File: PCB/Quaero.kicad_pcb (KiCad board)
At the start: 2 copper layers, 170.5 x 135.2 mm, 61 parts, among them J1 USB_C_Receptacle_USB2.0_16P, J2 OLED_128x32, J5 Conn_01x02, SW2 SW_SPDT

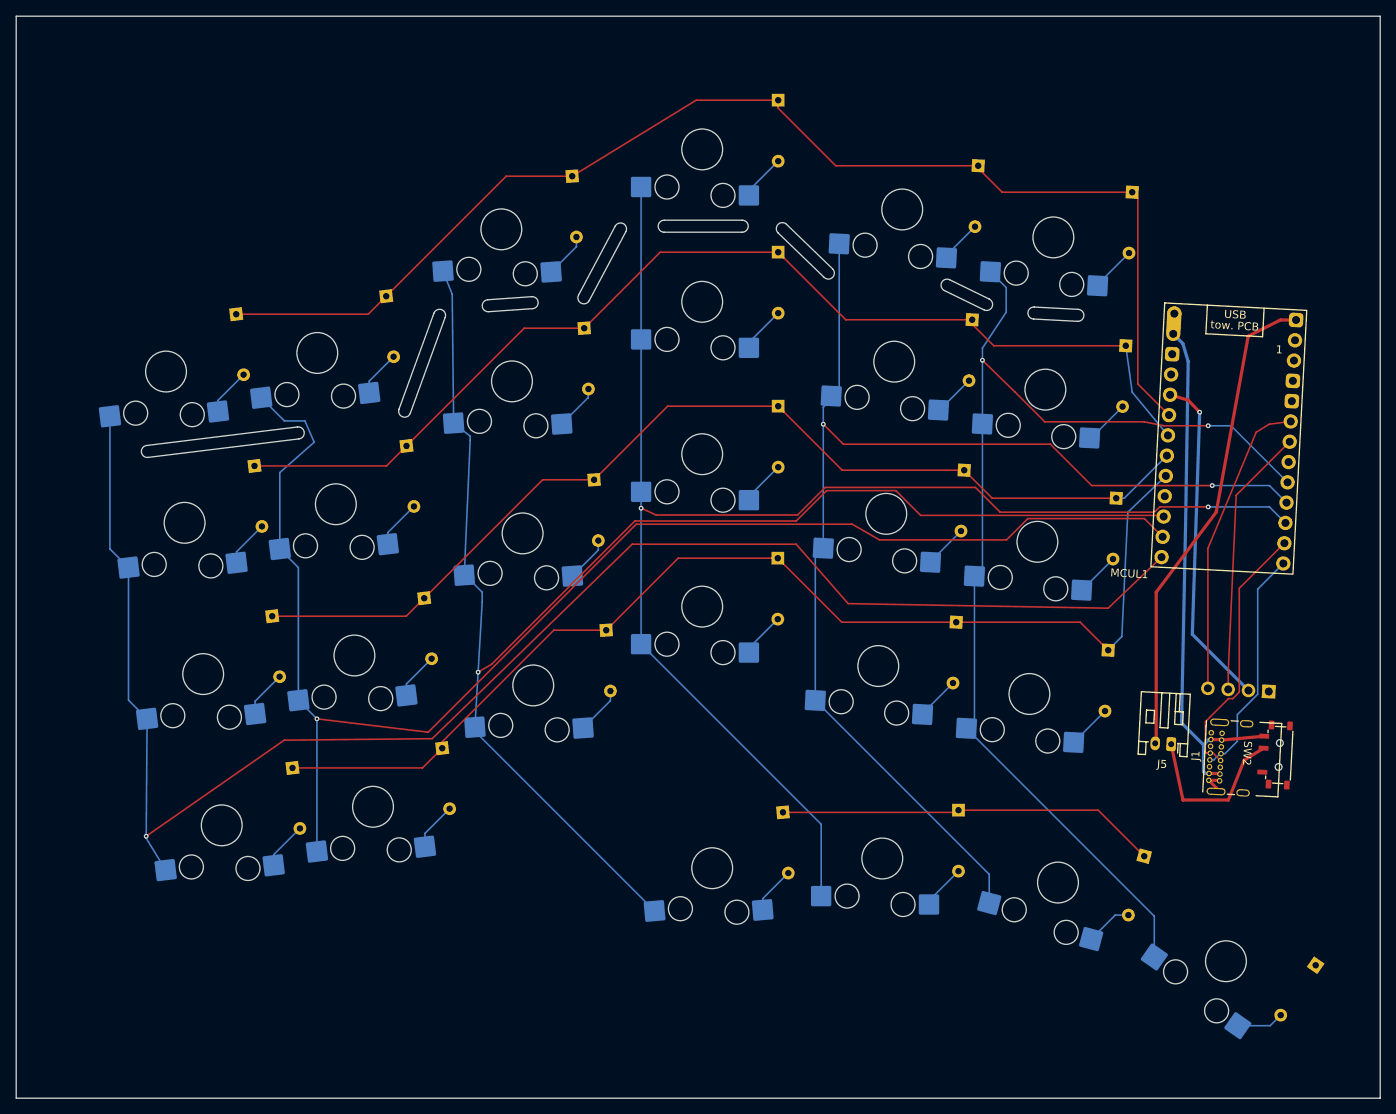
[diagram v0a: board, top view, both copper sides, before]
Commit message: Left side partial routing attempt 4
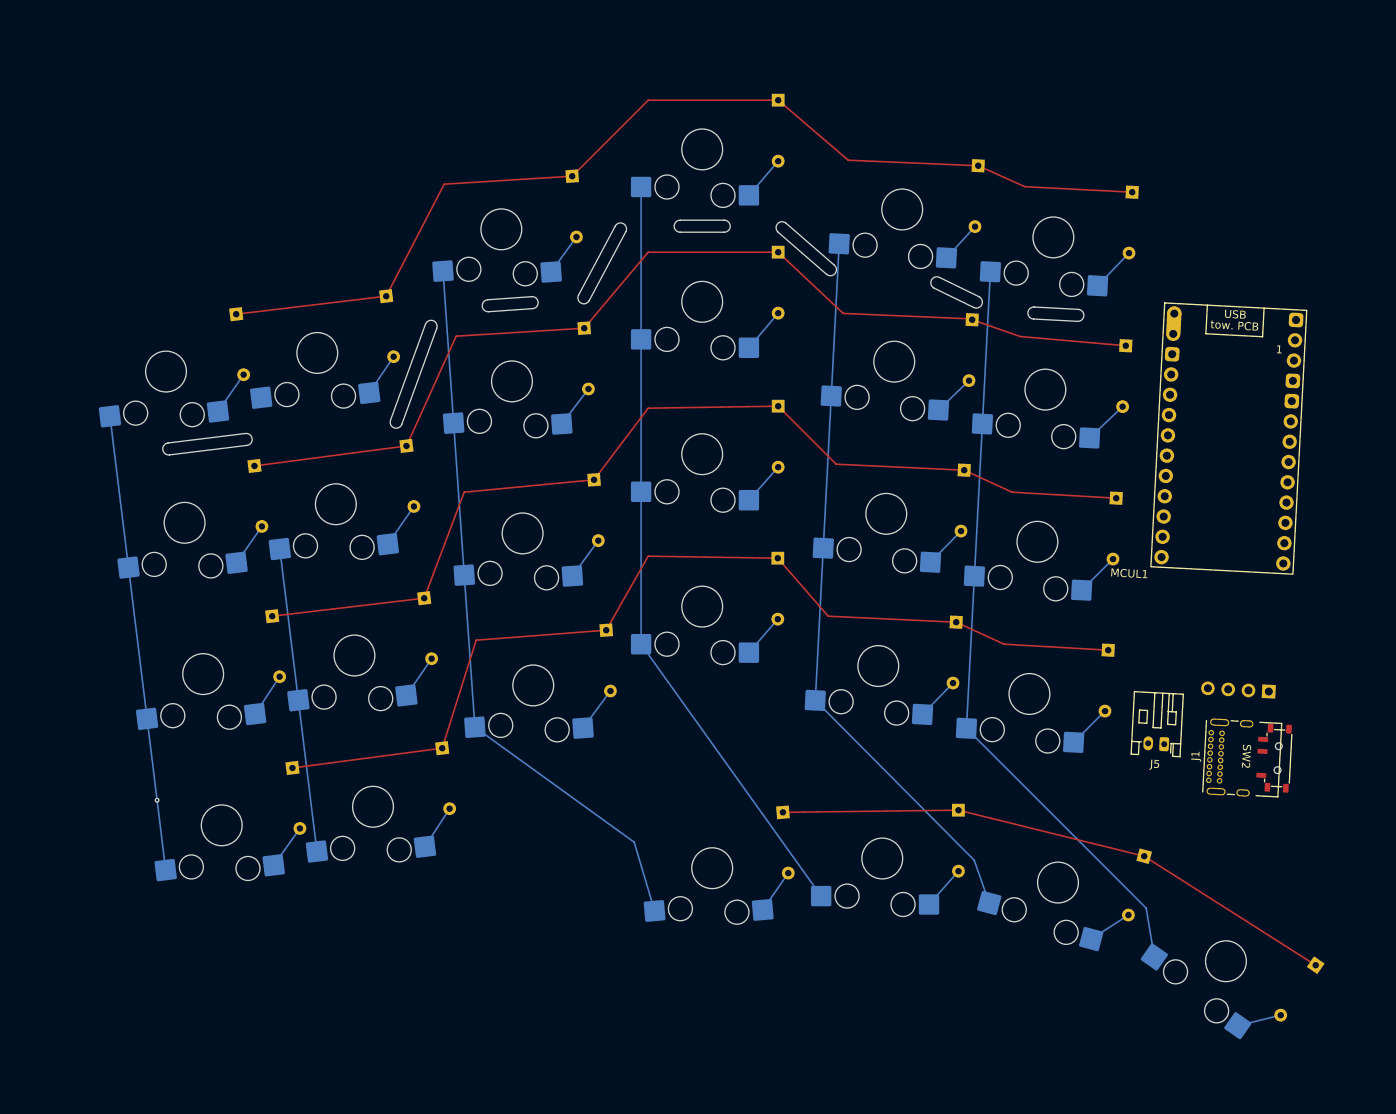
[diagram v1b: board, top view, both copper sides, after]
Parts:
- moved J5 0.87 mm to (153.0, 131.5)
- moved SW2 0.42 mm to (167.2, 133.2)
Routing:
- net LCol-1: track 205.8 -> 57.1 mm
- net LCol-2: track 183.7 -> 38.1 mm, vias 1 -> 0
- net LCol-3: track 187.8 -> 90.7 mm, vias 1 -> 0
- net LCol-4: track 182.6 -> 95.9 mm, vias 2 -> 0
- net PWR_Positive: track 66.6 -> 0.00 mm
- net LCol-5: track 154.6 -> 91.0 mm, vias 2 -> 0
- net PWR_Negative: track 60.5 -> 0.00 mm
- net LCol-6: track 142.2 -> 95.1 mm, vias 2 -> 0
- net +3.3V: track 42.1 -> 0.00 mm, vias 1 -> 0
- net Net-(J2-SDA): track 37.8 -> 0.00 mm
- net Net-(J2-SCL): track 33.7 -> 0.00 mm
- net RX: track 33.0 -> 0.00 mm
- net LRow-1: track 157.1 -> 128.0 mm
- net TX: track 29.0 -> 0.00 mm
- net LRow-5: track 47.6 -> 71.3 mm
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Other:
- board size 170.5 x 135.2 mm -> 115.1 x 29.3 mm

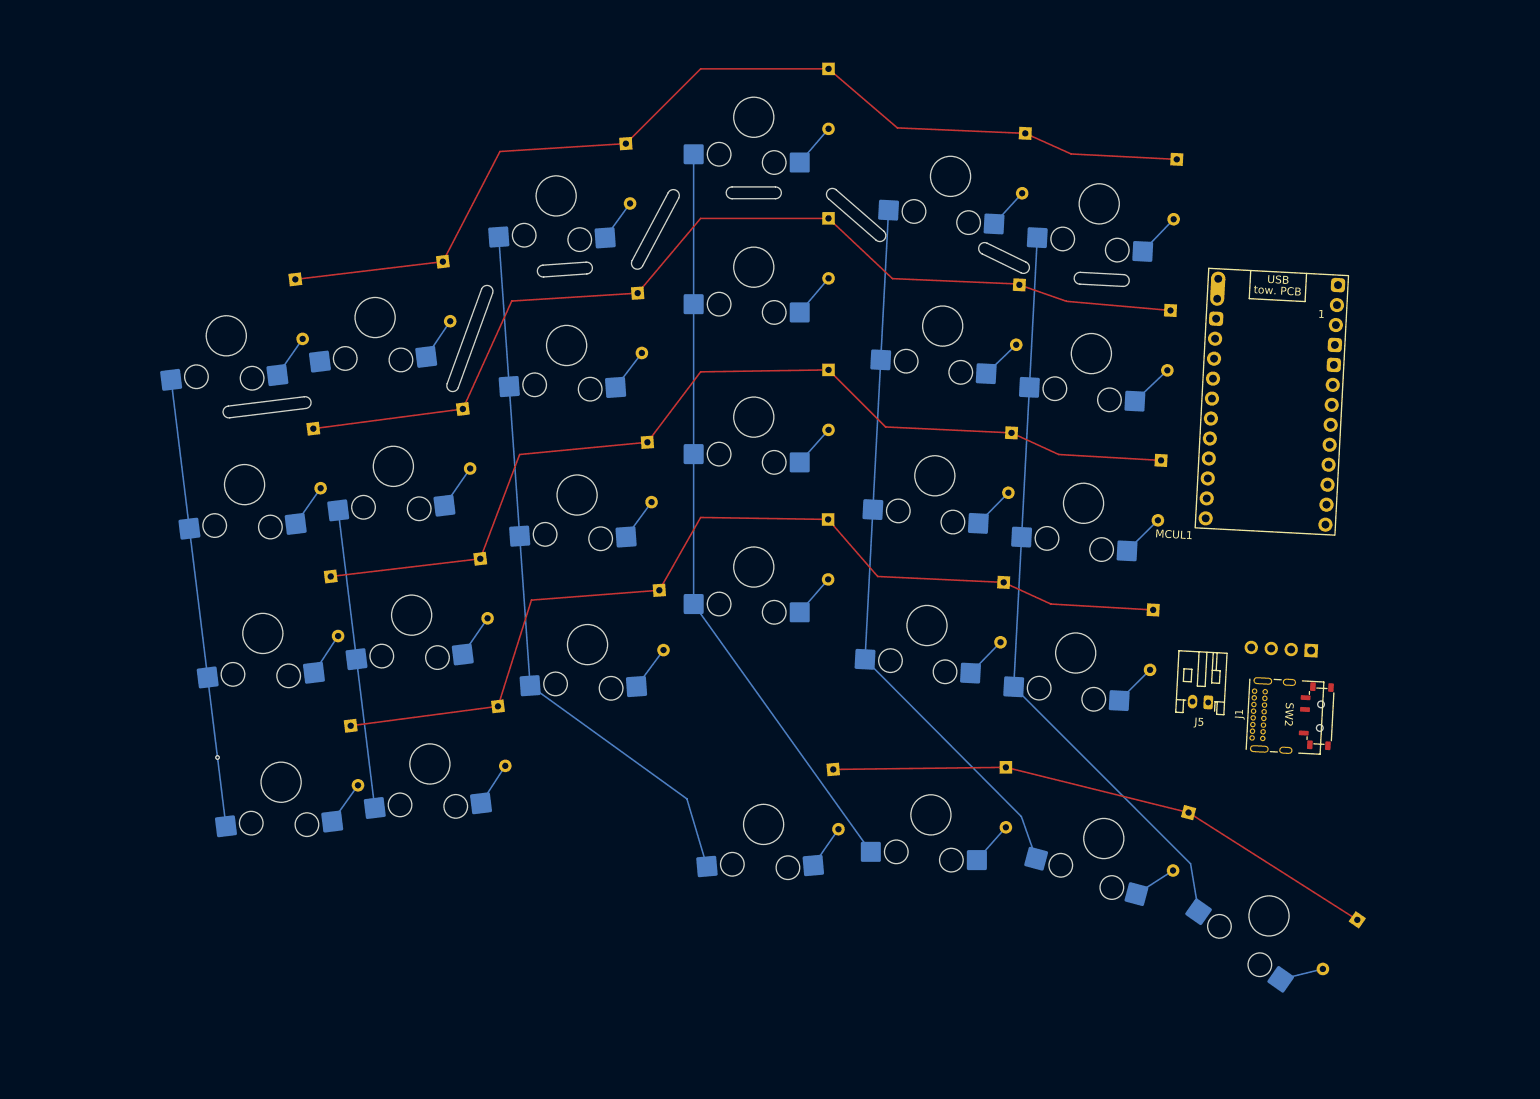
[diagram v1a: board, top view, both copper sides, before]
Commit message: Updated to RP2040, routing columns attempt 1
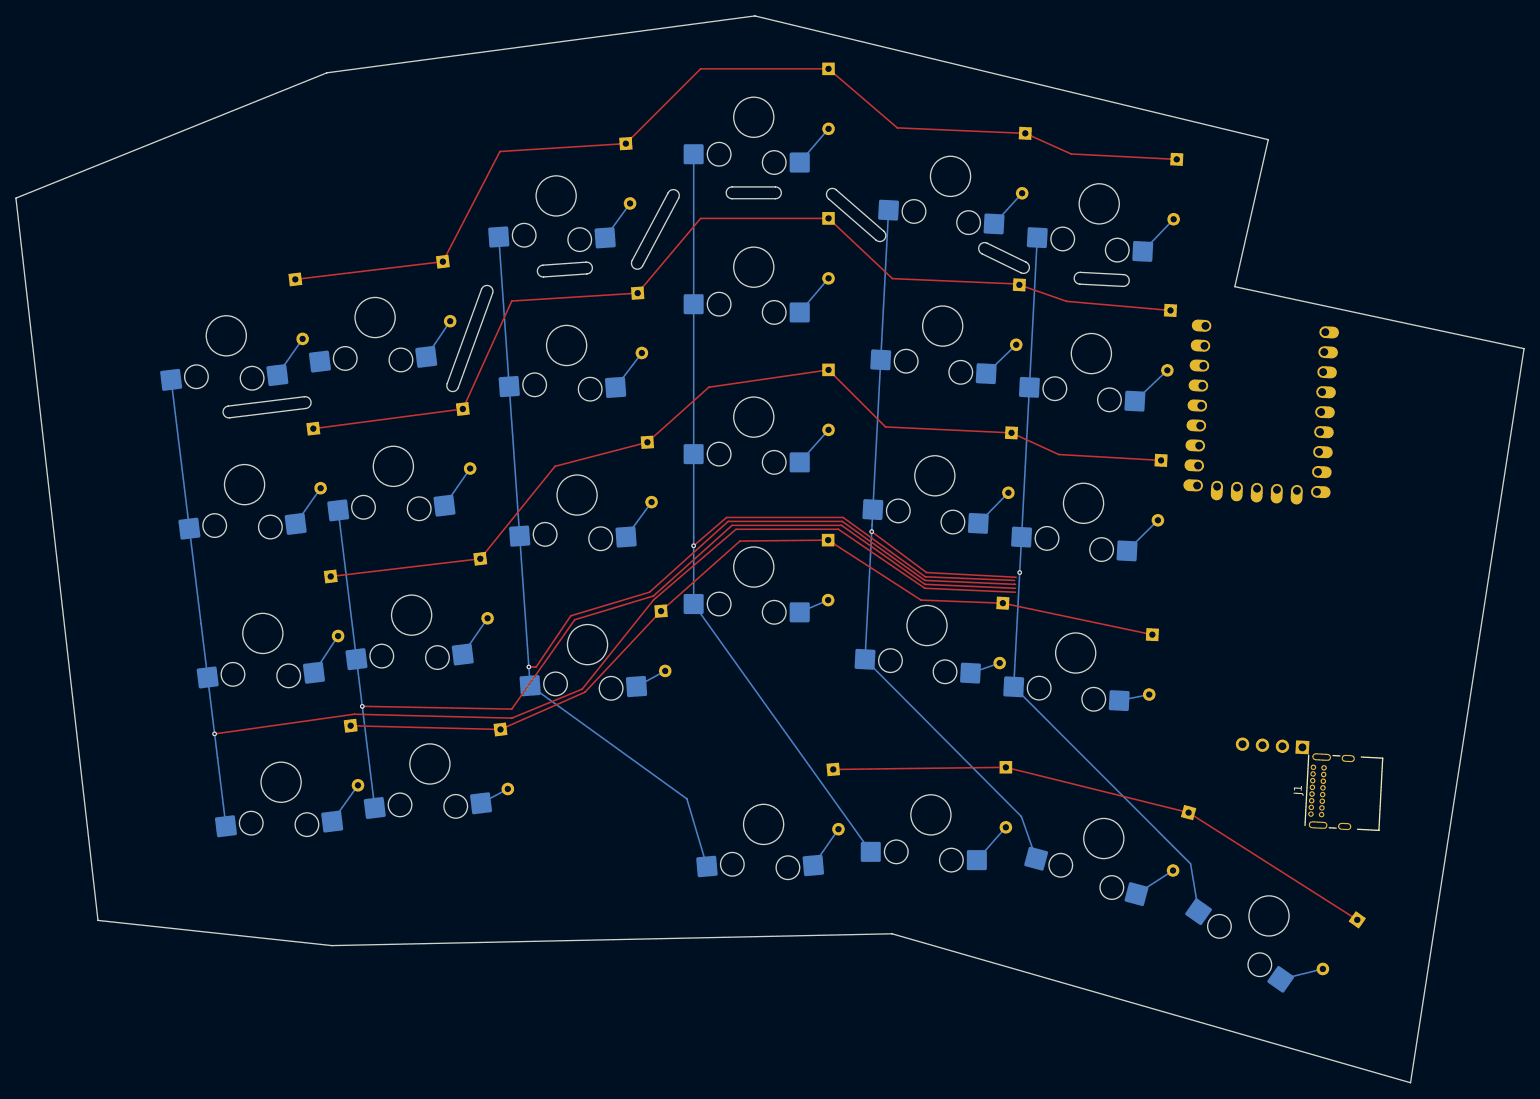
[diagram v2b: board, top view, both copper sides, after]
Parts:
- removed J5: Conn_01x02, Connector_JST:JST_PH_S2B-PH-K_1x02_P2.00mm_Horizontal
- removed MCUL1: SuperMini nRF52840, marbastlib-xp-promicroish:SuperMini_nRF52840_AH_USBdn
- removed SW2: SW_SPDT, marbastlib-various:SW_MSK12C02-HB
- added U1: RP2040_Zero, ScottoKeebs_MCU:RP2040_Zero, F.Cu at (159.7, 94.2)
- moved J2 12.3 mm to (155.1, 138.3)
- moved J1 12.2 mm to (166.0, 145.7)
- moved D24 3.14 mm to (145.9, 122.9)
- moved D20 2.95 mm to (63.1, 134.9)
- moved D21 2.66 mm to (83.5, 119.9)
- moved D23 2.64 mm to (126.9, 118.9)
- moved D22 2.63 mm to (104.7, 110.9)
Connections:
- net PWR_Positive renamed +5V
- J2 pad 3: Net-(J2-SCL) -> SCL
- J2 pad 4: Net-(J2-SDA) -> SDA
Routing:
- net LCol-1: track 57.1 -> 170.9 mm
- net LCol-2: track 38.1 -> 133.3 mm, vias 0 -> 1
- net LCol-3: track 90.7 -> 162.3 mm, vias 0 -> 1
- net LCol-4: track 95.9 -> 140.4 mm, vias 0 -> 1
- net LCol-5: track 91.0 -> 111.1 mm, vias 0 -> 1
- net LRow-4: track 121.4 -> 113.4 mm
- net LRow-3: track 123.0 -> 118.1 mm
- net Net-(D20-A): track 5.67 -> 3.86 mm
- net Net-(D24-A): track 5.54 -> 3.89 mm
- net Net-(D21-A): track 5.76 -> 4.15 mm
- net Net-(D22-A): track 5.52 -> 3.93 mm
- net Net-(D23-A): track 5.47 -> 3.92 mm
- net LCol-6: vias 0 -> 1
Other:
- board size 115.1 x 29.3 mm -> 191.6 x 135.5 mm

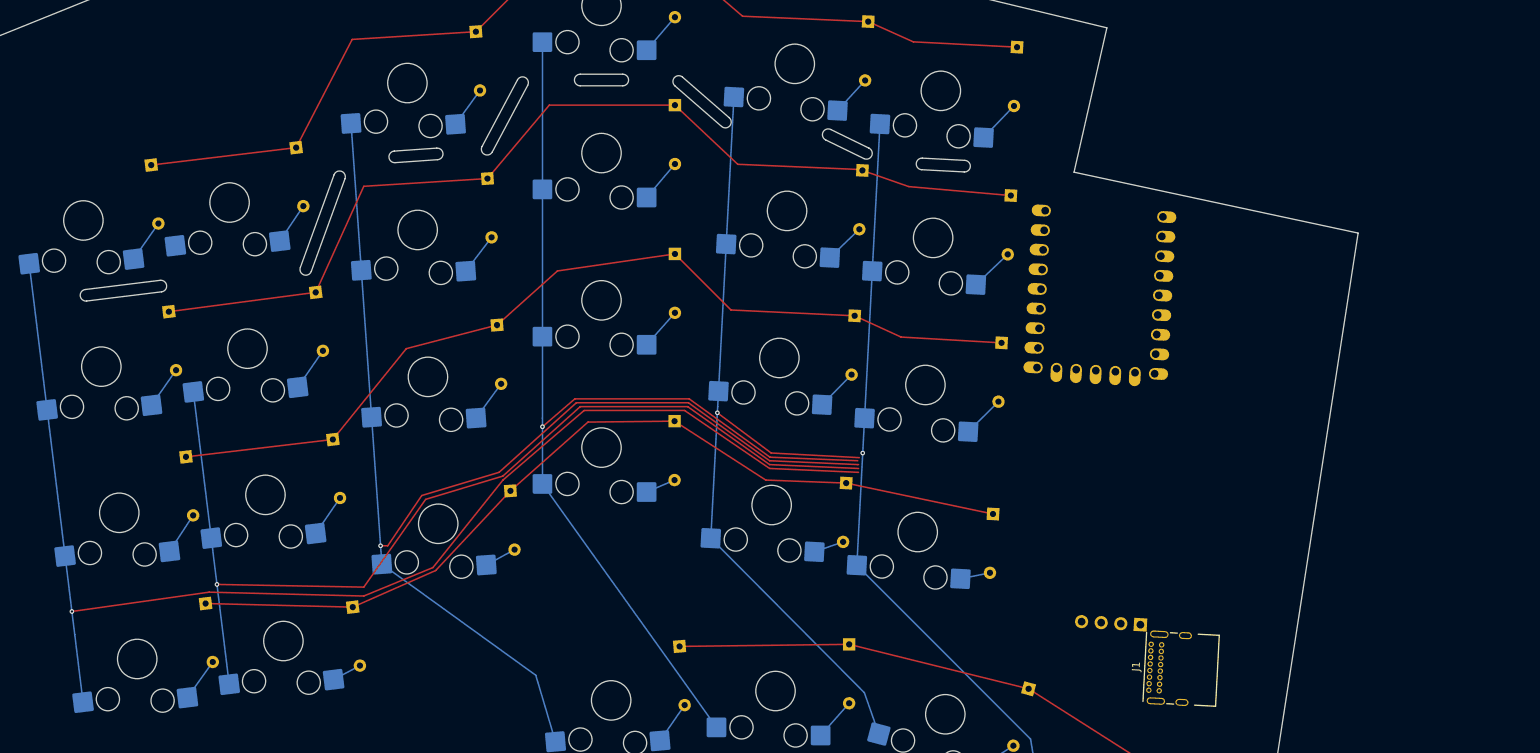
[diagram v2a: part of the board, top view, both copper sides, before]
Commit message: Revised routing, changed the MCU to the RP2040 Zero, changed the USB-C schematic
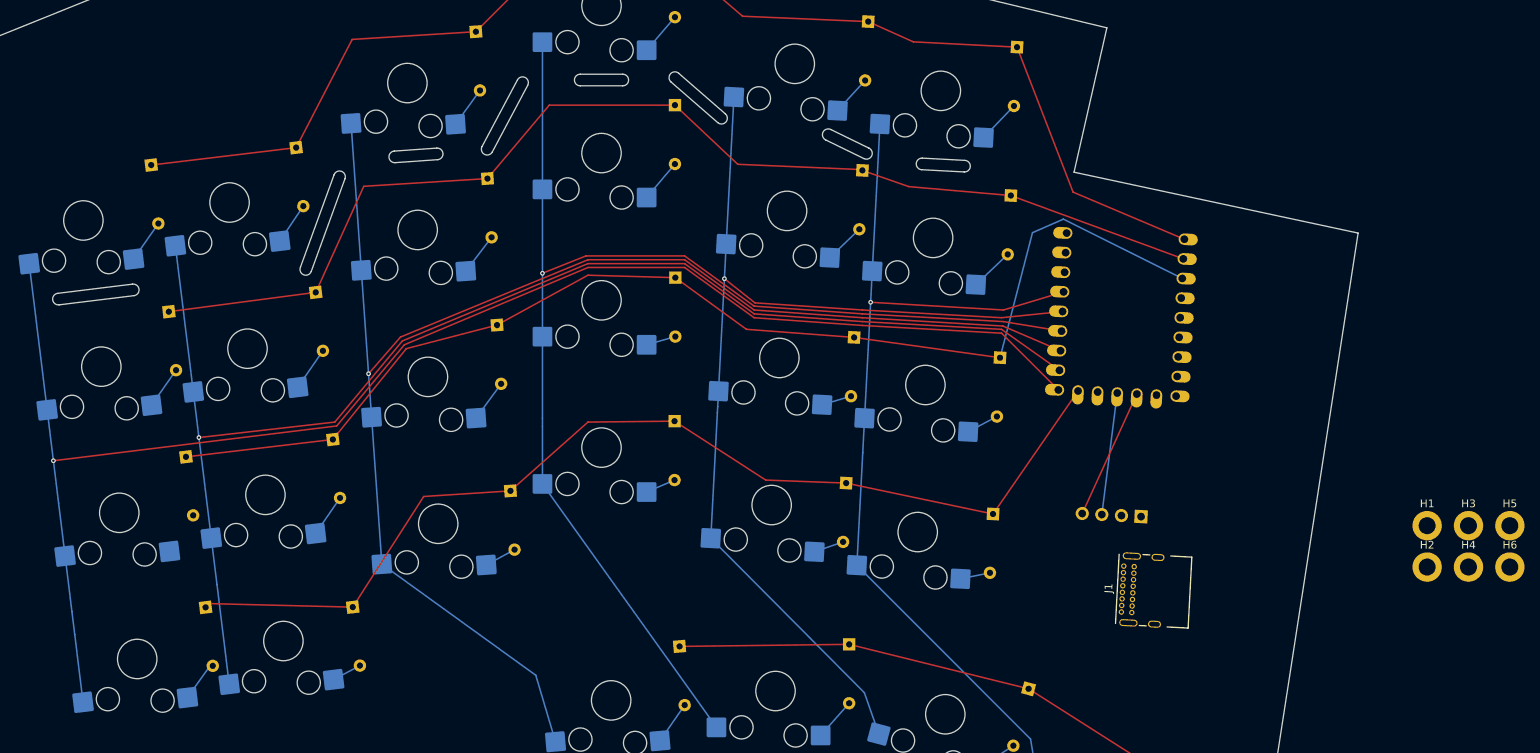
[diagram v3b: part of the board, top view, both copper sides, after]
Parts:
- added H1: MountingHole_Pad, MountingHole:MountingHole_2.2mm_M2_DIN965_Pad, F.Cu at (202.1, 124.4)
- added H2: MountingHole_Pad, MountingHole:MountingHole_2.2mm_M2_DIN965_Pad, F.Cu at (202.1, 129.8)
- added H3: MountingHole_Pad, MountingHole:MountingHole_2.2mm_M2_DIN965_Pad, F.Cu at (207.4, 124.4)
- added H4: MountingHole_Pad, MountingHole:MountingHole_2.2mm_M2_DIN965_Pad, F.Cu at (207.4, 129.8)
- added H5: MountingHole_Pad, MountingHole:MountingHole_2.2mm_M2_DIN965_Pad, F.Cu at (212.8, 124.4)
- added H6: MountingHole_Pad, MountingHole:MountingHole_2.2mm_M2_DIN965_Pad, F.Cu at (212.8, 129.8)
- moved J2 14.0 mm to (155.2, 124.3)
- moved J1 10.7 mm to (162.5, 135.6)
- moved U1 4.01 mm to (162.5, 97.1)
- moved D16 3.07 mm to (104.8, 92.3)
- moved D17 2.80 mm to (127.9, 100.0)
- moved D18 1.93 mm to (146.8, 102.7)
- moved D19 0.50 mm to (44.0, 135.0)
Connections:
- J1 pad A6: TX -> unconnected-(J1-D+-PadA6)
- J1 pad A7: RX -> unconnected-(J1-D--PadA7)
- J1 pad A8: unconnected-(J1-SBU1-PadA8) -> TX
- J1 pad B6: TX -> unconnected-(J1-D+-PadB6)
- J1 pad B7: RX -> unconnected-(J1-D--PadB7)
- J1 pad B8: unconnected-(J1-SBU2-PadB8) -> TX
- U1 pad 15: LCol-6 -> LCol-1
- U1 pad 16: LCol-5 -> LCol-2
- U1 pad 17: LCol-4 -> LCol-3
- U1 pad 18: LCol-3 -> LCol-4
- U1 pad 19: LCol-2 -> LCol-5
- U1 pad 20: LCol-1 -> LCol-6
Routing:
- net LCol-2: track 133.3 -> 179.4 mm
- net LRow-1: track 128.0 -> 163.7 mm
- net LRow-3: track 118.1 -> 153.7 mm
- net LCol-1: track 170.9 -> 199.6 mm
- net LCol-6: track 95.1 -> 120.5 mm
- net LCol-4: track 140.4 -> 165.7 mm
- net LCol-3: track 162.3 -> 187.2 mm
- net LCol-5: track 111.1 -> 135.9 mm
- net LRow-2: track 126.0 -> 149.7 mm
- net LRow-4: track 113.4 -> 135.1 mm
- net SDA: track 0.00 -> 17.0 mm
- net SCL: track 0.00 -> 15.8 mm
- net Net-(D13-A): track 5.58 -> 0.00 mm
- net Net-(D16-A): track 5.52 -> 3.86 mm
- net Net-(D17-A): track 5.45 -> 3.90 mm
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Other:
- outline, holes or cut-outs redrawn
